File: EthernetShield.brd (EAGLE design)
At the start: 68.6 x 53.3 mm, 74 parts, among them IC1 W5100SQFP80, IC2 MCP24AA025E48, Q1 2N7002, SW1 RESET

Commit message: Updates for release v2.0
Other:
- board text added: "Ethernet Shield"
- board text added: "v2.0 SKU: ES"
- board text added: "www.freetronics.com/es"
- board text removed: "Ethernet Shield R3"
- board text removed: "SKU: SH-ETHERNET"
- board text removed: "v2.0"
- board text removed: "www.freetronics.com/ethernet"
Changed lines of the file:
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@@
 <setting verticaltext="up"/>
 </settings>
-<grid distance="0.01" unitdist="inch" unit="inch" style="lines" multiple="1" display="yes" altdistance="0.005" altunitdist="inch" altunit="inch"/>
+<grid distance="0.05" unitdist="inch" unit="inch" style="lines" multiple="1" display="no" altdistance="0.005" altunitdist="inch" altunit="inch"/>
 <layers>
 <layer number="1" name="Top" color="4" fill="1" visible="yes" active="yes"/>
@@
 <circle x="2.032" y="35.814" radius="1.016" width="1.016" layer="41"/>
 <circle x="48.26" y="5.588" radius="1.016" width="1.016" layer="41"/>
-<text x="25.908" y="29.718" size="1.27" layer="22" font="vector" ratio="16" rot="SMR270">(c) 2013 Freetronics</text>
+<text x="23.368" y="33.528" size="1.27" layer="22" font="vector" ratio="16" rot="SMR270">(c) 2013 Freetronics</text>
 <text x="19.685" y="0.7366" size="1.016" layer="21" font="vector" ratio="15">RESET</text>
 <text x="46.6852" y="8.636" size="1.27" layer="21" font="vector" ratio="16">GND</text>
@@
 <text x="23.622" y="48.387" size="0.8128" layer="21" font="vector" ratio="15">A</text>
 <text x="25.4" y="48.26" size="0.8128" layer="21" font="vector" ratio="15">GND</text>
-<text x="67.6402" y="5.8674" size="1.1684" layer="21" font="vector" ratio="17" rot="R90">Ethernet Shield R3</text>
+<text x="67.6402" y="7.3914" size="1.1684" layer="21" font="vector" ratio="17" rot="R90">Ethernet Shield</text>
 <text x="30.1244" y="42.9006" size="1.27" layer="22" font="vector" ratio="18" rot="SMR270">5V</text>
 <text x="46.609" y="5.08" size="0.8128" layer="22" font="vector" ratio="15" rot="MR0">VIN</text>
@@
 <text x="24.1046" y="18.161" size="1.27" layer="21" ratio="18" rot="R90">!</text>
 <text x="22.606" y="13.0302" size="1.6764" layer="21" ratio="18" rot="R90">PoE</text>
-<text x="27.94" y="9.144" size="0.762" layer="21" font="vector" ratio="15">www.freetronics.com/ethernet</text>
+<text x="27.178" y="9.144" size="1.016" layer="21" font="vector" ratio="15">www.freetronics.com/es</text>
 <text x="19.05" y="8.3312" size="0.8128" layer="21" font="vector" ratio="17">freetronics</text>
 <text x="29.8704" y="13.1826" size="1.27" layer="22" font="vector" ratio="18" rot="SMR270">GND</text>
 <text x="17.145" y="38.1" size="1.016" layer="21" ratio="15">RST</text>
 <text x="17.145" y="39.37" size="1.016" layer="21" ratio="15">WIZ</text>
-<text x="21.844" y="40.894" size="1.4224" layer="22" font="vector" ratio="16" rot="SMR270">www.freetronics.com/ethernet</text>
+<text x="21.336" y="35.56" size="1.4224" layer="22" font="vector" ratio="16" rot="SMR270">www.freetronics.com/es</text>
 <text x="26.416" y="43.053" size="1.27" layer="22" font="vector" ratio="16" rot="SMR270">freetronics</text>
-<text x="24.003" y="26.543" size="1.27" layer="22" font="vector" ratio="16" rot="SMR270">SKU: SH-ETHERNET</text>
+<text x="18.415" y="1.905" size="1.27" layer="22" font="vector" ratio="16" rot="SMR0">v2.0    SKU: ES</text>
 <rectangle x1="32.766" y1="5.207" x2="33.274" y2="6.35" layer="21"/>
 <rectangle x1="35.306" y1="3.81" x2="35.814" y2="4.953" layer="21"/>
@@
 <text x="22.352" y="48.26" size="0.8128" layer="22" font="vector" ratio="15" rot="MR0">SDA</text>
 <text x="19.812" y="47.371" size="0.8128" layer="22" font="vector" ratio="15" rot="MR0">SCL</text>
-<text x="66.1162" y="4.5974" size="1.1684" layer="21" font="vector" ratio="17" rot="R90">v2.0</text>
 <wire x1="62.992" y1="31.75" x2="62.23" y2="30.988" width="0.254" layer="22"/>
 <wire x1="62.23" y1="24.892" x2="62.992" y2="24.13" width="0.254" layer="22"/>

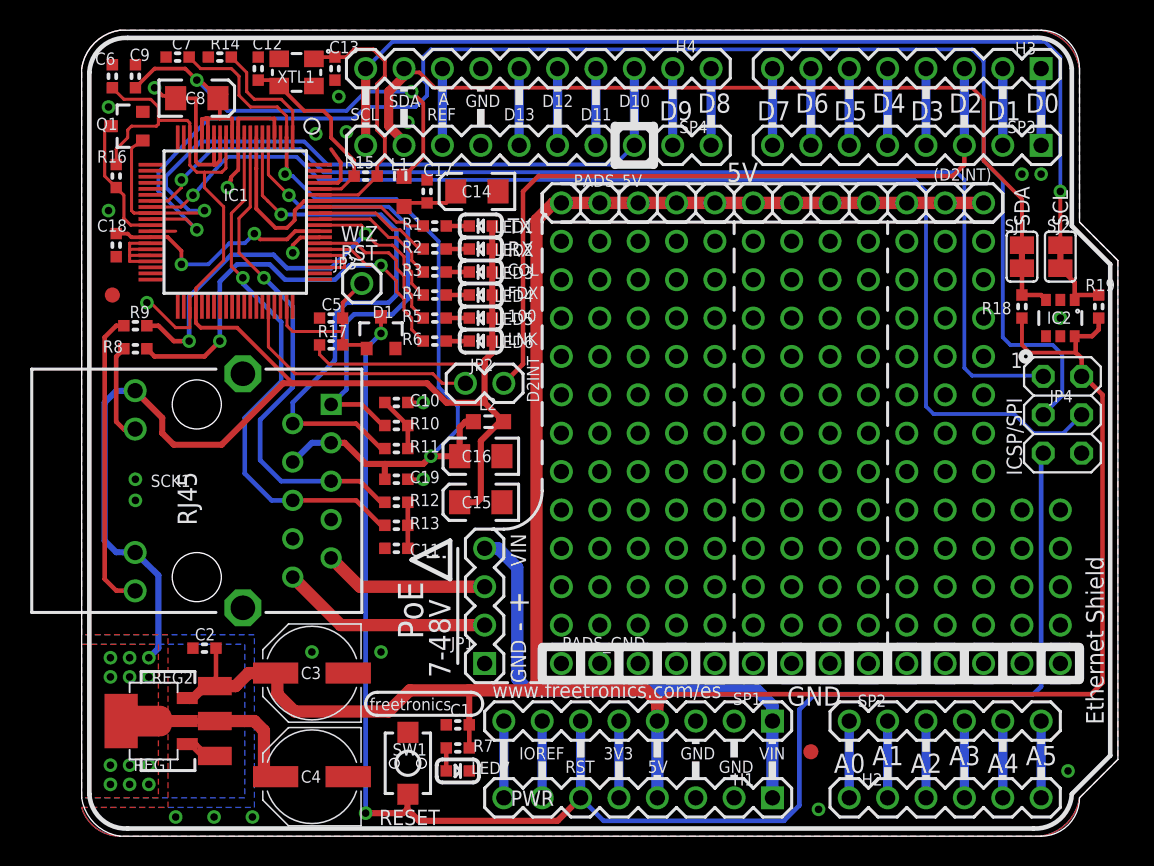
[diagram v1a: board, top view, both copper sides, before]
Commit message: Changed I2C pull-ups to use IOREF, and added isolation jumpers
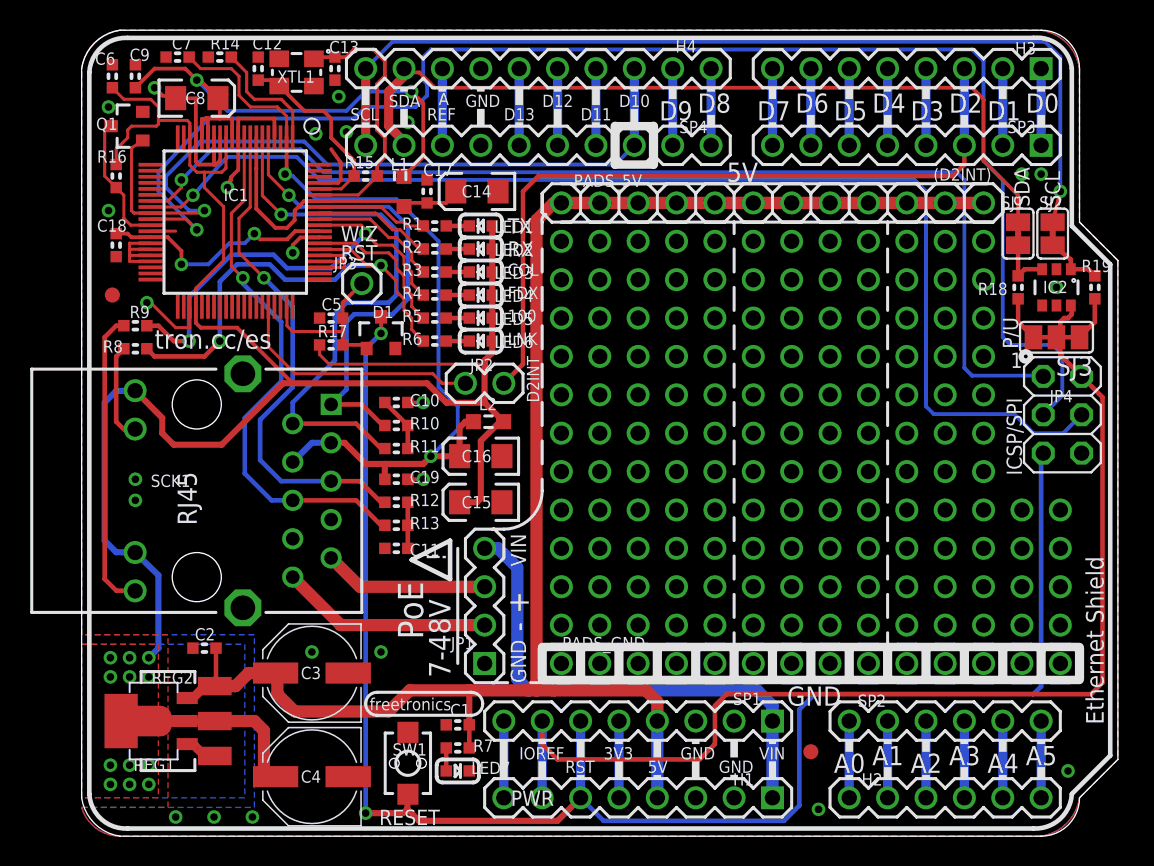
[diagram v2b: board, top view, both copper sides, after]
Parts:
- added SJ3: (no value), freetronics-original:SJ_2
- moved IC2 2.05 mm to (64.5, 36.3)
- moved SJ2 1.61 mm to (64.3, 39.9)
- moved SJ1 1.55 mm to (62.0, 39.9)
- moved R19 1.30 mm to (67.1, 36.3)
- moved R18 1.30 mm to (62.0, 36.3)
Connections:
- new net N$53: R19.1, SJ3.1
- new net N$7: R18.1, SJ3.3
- net 5V: no longer IC2.6, JP4.2, R18.1, R19.1
- net IOREF: now also IC2.6, JP4.2, SJ3.2
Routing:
- net IOREF: track 5.08 -> 74.6 mm
- net 5V: track 175.2 -> 113.3 mm
- net N$7: track 0.00 -> 4.48 mm
- net N$53: track 0.00 -> 4.48 mm
- net SDA: track 55.8 -> 54.2 mm
- net SCL: track 64.7 -> 63.2 mm
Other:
- board text added: "P/U"
- board text added: "tron.cc/es"

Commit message: Added info about I2C address
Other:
- board text added: "(c) 2014 Freetronics Pty Ltd"
- board text removed: "(c) 2013 Freetronics"
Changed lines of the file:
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@@
 <circle x="2.032" y="35.814" radius="1.016" width="1.016" layer="41"/>
 <circle x="48.26" y="5.588" radius="1.016" width="1.016" layer="41"/>
-<text x="23.368" y="33.528" size="1.27" layer="22" font="vector" ratio="16" rot="SMR270">(c) 2013 Freetronics</text>
+<text x="23.368" y="37.846" size="1.27" layer="22" font="vector" ratio="16" rot="SMR270">(c) 2014 Freetronics Pty Ltd</text>
 <text x="19.685" y="0.7366" size="1.016" layer="21" font="vector" ratio="15">RESET</text>
 <text x="46.6852" y="8.636" size="1.27" layer="21" font="vector" ratio="16">GND</text>

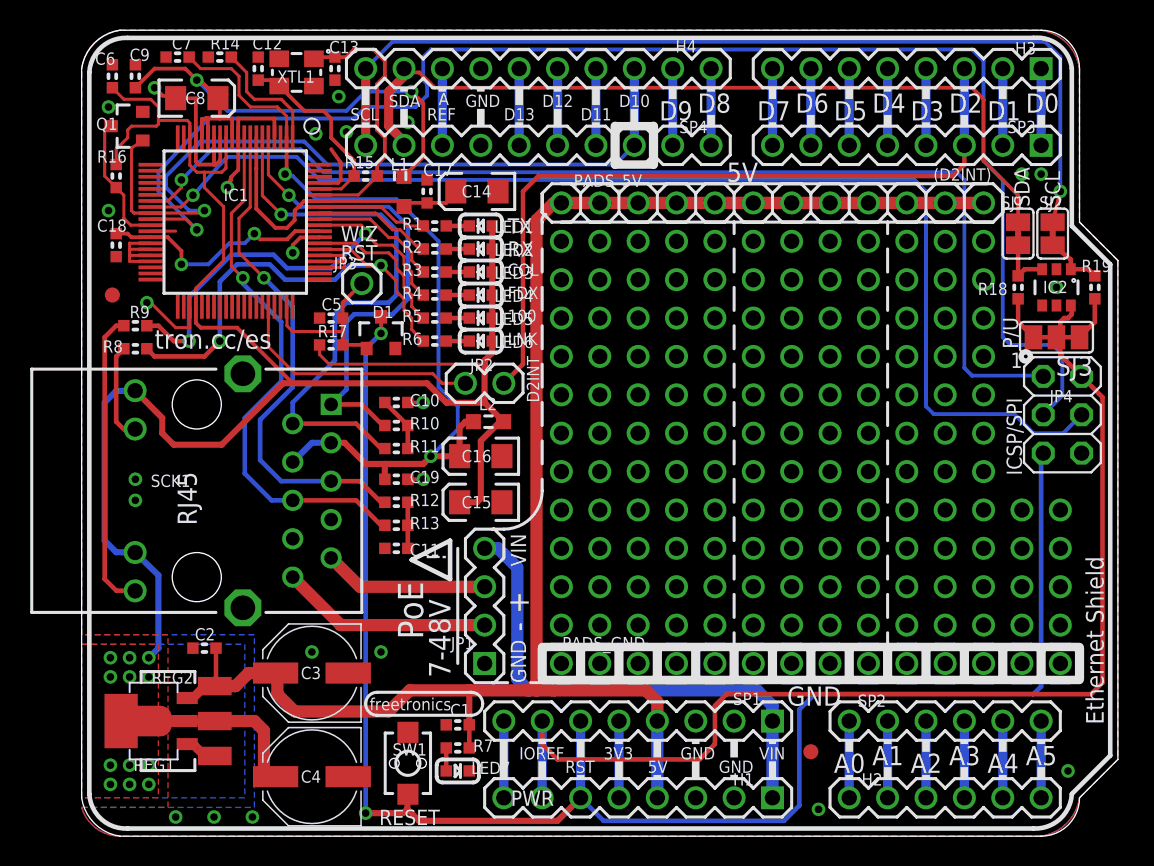
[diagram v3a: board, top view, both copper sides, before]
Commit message: Began replacing W5100 with W5500
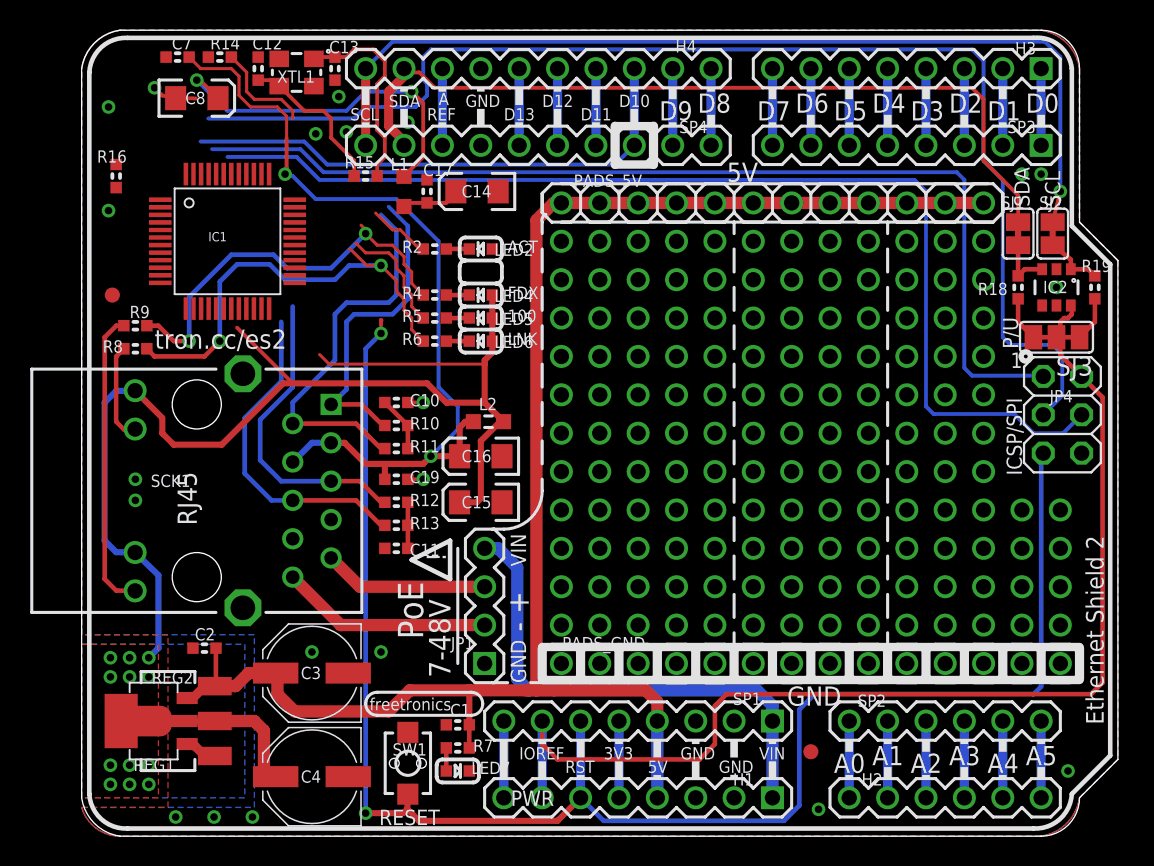
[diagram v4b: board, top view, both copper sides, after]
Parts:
- removed C18, C6, C9: 100nF, freetronics:0603
- removed C5: 47nF, freetronics:0603
- removed D1: BAT54 SCHOTTKY, freetronics:SOT23-3
- removed JP2: D2_INT, freetronics:1X02
- removed JP3: (no value), freetronics:1X01
- removed LED1: YELLOW, freetronics:LED-0603
- removed LED3: RED, freetronics:LED-0603
- removed Q1: 2N7002, freetronics:SOT23-3
- removed R1, R3: 1K, freetronics:0603
- removed R17: 10K, freetronics:0603
- IC1: value W5100SQFP80 -> W5500; device freetronics-marc:SQFP80 -> W5500:W5500
- R16: value 1K -> 10K
- moved IC1 1.37 mm to (9.65, 39.4), turned to 0 degrees
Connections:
- removed net 1V8OUT: C18.1, IC1.33, IC1.69
- removed net COLLED: IC1.71, R3.2
- removed net N$322: IC1.1, R14.2
- removed net N$328: LED3.C, R3.1
- removed net N$330: LED1.C, R1.1
- removed net N$70: C5.1, D1.1, IC1.59, JP3.1, R17.2
- removed net RXLED: IC1.72, R2.2
- removed net SEN: IC1.31, Q1.3, R16.1
- removed net TXLED: IC1.73, R1.2
- new net ACTLED: IC1.27, R2.2
- new net EXRES1: IC1.10, R14.2
- new net N$66: IC1.31
- new net N$71: IC1.30
- net 1V8A: no longer IC1.7, IC1.74
- net 1V8_OUT: no longer C9.1, IC1.11, IC1.15, IC1.16
- net 3V3A: no longer IC1.2
- net 3V3D: no longer C6.1, IC1.12, IC1.18, IC1.44, LED1.A, LED3.A, R17.1
- net D10_SS: now also IC1.32, R16.1; no longer IC1.29, Q1.1
- net D2: no longer JP2.1
- net FDXLED: now also IC1.26; no longer IC1.70
- net GND: now also IC1.16, IC1.19, IC1.3, IC1.48, IC1.9; no longer C18.2, C5.2, C6.2, C9.2, IC1.10, IC1.13, IC1.17, IC1.32, IC1.34, IC1.35, IC1.36, IC1.37, IC1.4, IC1.43, IC1.63, IC1.64, IC1.65, IC1.68, IC1.77, Q1.2
- net INT: now also IC1.36; no longer IC1.56, JP2.2
- net LINKLED: now also IC1.25; no longer IC1.66
- net MISO: now also IC1.34; no longer IC1.27
- net MOSI: now also IC1.35; no longer IC1.28
- net RESET: no longer D1.3
- net RXIN: now also IC1.5; no longer IC1.6
- net RXIP: now also IC1.6; no longer IC1.5
- net SCK: now also IC1.33; no longer IC1.30
- net SPDLED: now also IC1.24; no longer IC1.67
- net TXON: now also IC1.1; no longer IC1.9
- net TXOP: now also IC1.2; no longer IC1.8
- net XTLN: no longer IC1.75
- net XTLP: no longer IC1.76
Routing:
- net D2: track 49.5 -> 5.08 mm
- net GND: track 50.7 -> 7.19 mm, vias 24 -> 21
- net 3V3D: track 132.7 -> 94.1 mm
- net D10_SS: track 52.1 -> 34.9 mm, vias 1 -> 0
- net INT: track 16.7 -> 0.00 mm
- net 1V8OUT: track 16.1 -> 0.00 mm, vias 2 -> 0
- net 1V8A: track 20.3 -> 4.53 mm
- net TXON: track 35.6 -> 21.7 mm, vias 1 -> 0
- net SCK: track 96.2 -> 83.1 mm, vias 1 -> 0
- net TXOP: track 33.4 -> 20.5 mm, vias 1 -> 0
- net 1V8_OUT: track 37.4 -> 25.1 mm
- net RXIN: track 37.7 -> 25.5 mm, vias 1 -> 0
- net N$70: track 11.5 -> 0.00 mm
- net RXIP: track 32.6 -> 21.3 mm, vias 1 -> 0
- net SEN: track 8.93 -> 0.00 mm
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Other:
- board text added: "ACT"
- board text added: "Ethernet Shield 2"
- board text added: "tron.cc/es2"
- board text removed: "(D2INT)"
- board text removed: "COL"
- board text removed: "D2INT"
- board text removed: "Ethernet Shield"
- board text removed: "RX"
- board text removed: "TX"
- board text removed: "WIZ"
- board text removed: "tron.cc/es"
